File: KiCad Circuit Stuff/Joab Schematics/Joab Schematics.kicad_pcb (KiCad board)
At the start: 2 copper layers, 56 parts, among them J1 Conn_02x16_Odd_Even, J2 Conn_01x02, Q1 S8550, Q2 MMBT3904, U1 MT3608, U2 AMS1117-3.3, U3 TP4056, U4 INA219AIDCNR, U6 TS5A3159DCKR, U7 TPS5430DDAR

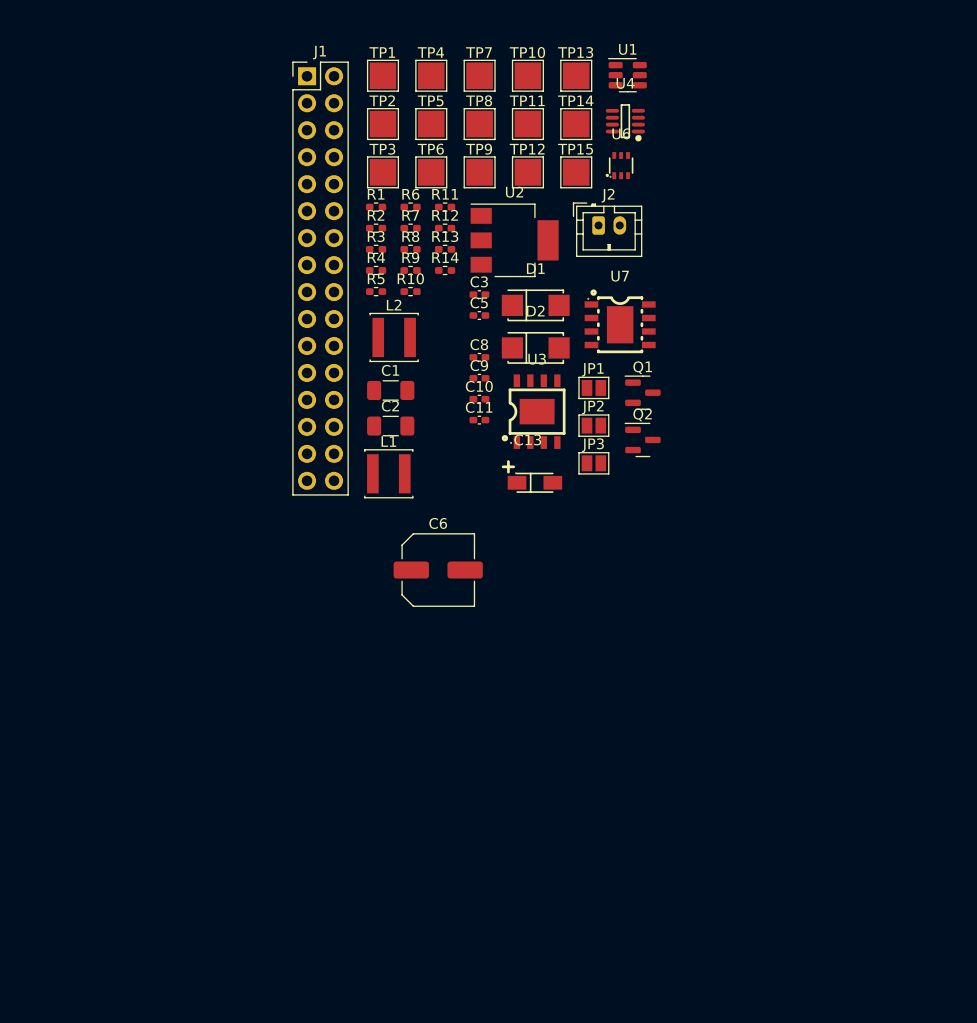
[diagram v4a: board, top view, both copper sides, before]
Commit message: Chose all passive components, added test points to all
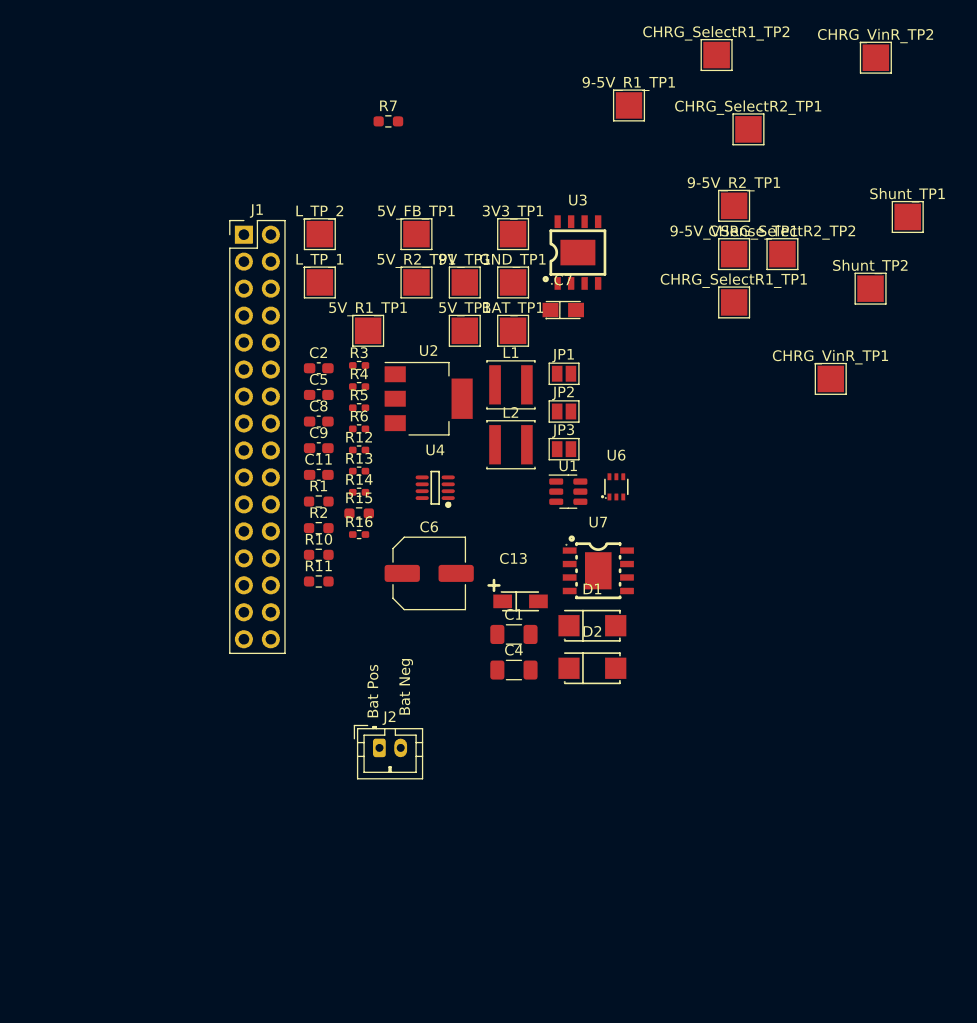
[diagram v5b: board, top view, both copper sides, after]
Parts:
- removed C10, C3: 10u, Capacitor_SMD:C_0402_1005Metric_Pad0.74x0.62mm_HandSolder
- removed Q1: S8550, Package_TO_SOT_SMD:SOT-23
- removed Q2: MMBT3904, Package_TO_SOT_SMD:SOT-23
- removed R8: 2k, Resistor_SMD:R_0402_1005Metric_Pad0.72x0.64mm_HandSolder
- removed R9: 1000k, Resistor_SMD:R_0402_1005Metric_Pad0.72x0.64mm_HandSolder
- removed TP1: L TP 2, TestPoint:TestPoint_Pad_2.5x2.5mm
- removed TP10, TP3, TP4, TP5, TP6, TP7, TP8, TP9: TestPoint, TestPoint:TestPoint_Pad_2.5x2.5mm
- removed TP11: 9V TP, TestPoint:TestPoint_Pad_2.5x2.5mm
- removed TP12: 5V TP, TestPoint:TestPoint_Pad_2.5x2.5mm
- removed TP13: 3V3 TP, TestPoint:TestPoint_Pad_2.5x2.5mm
- removed TP14: GND TP, TestPoint:TestPoint_Pad_2.5x2.5mm
- removed TP15: BAT TP, TestPoint:TestPoint_Pad_2.5x2.5mm
- removed TP2: L TP 1, TestPoint:TestPoint_Pad_2.5x2.5mm
- added 3V3_TP1: 3V3 TP, TestPoint:TestPoint_Pad_2.5x2.5mm, F.Cu at (174.6, 75.4)
- added 5V_FB_TP1: 5V FB TP, TestPoint:TestPoint_Pad_2.5x2.5mm, F.Cu at (165.5, 75.4)
- added 5V_R1_TP1: ~, TestPoint:TestPoint_Pad_2.5x2.5mm, F.Cu at (160.9, 84.5)
- added 5V_R2_TP1: 5V R2 TP, TestPoint:TestPoint_Pad_2.5x2.5mm, F.Cu at (165.5, 79.9)
- added 5V_TP1: 5V TP, TestPoint:TestPoint_Pad_2.5x2.5mm, F.Cu at (170.0, 84.5)
- added 9-5V_R1_TP1: 9-5V R1 TP, TestPoint:TestPoint_Pad_2.5x2.5mm, F.Cu at (185.5, 63.2)
- added 9-5V_R2_TP1: 9-5V R2 TP, TestPoint:TestPoint_Pad_2.5x2.5mm, F.Cu at (195.4, 72.7)
- added 9-5V_VSense_TP1: 9-5V VSense TP, TestPoint:TestPoint_Pad_2.5x2.5mm, F.Cu at (195.4, 77.2)
- added 9V_TP1: 9V TP, TestPoint:TestPoint_Pad_2.5x2.5mm, F.Cu at (170.0, 79.9)
- added BAT_TP1: BAT TP, TestPoint:TestPoint_Pad_2.5x2.5mm, F.Cu at (174.6, 84.5)
- added C4: 22u, Capacitor_SMD:C_1206_3216Metric_Pad1.33x1.80mm_HandSolder, F.Cu at (174.7, 116.4)
- added C7: CA45-A-10V-22UF-K, JLCPCB:CASE-A_3216, F.Cu at (179.3, 82.5)
- added CHRG_SelectR1_TP1: TestPoint, TestPoint:TestPoint_Pad_2.5x2.5mm, F.Cu at (195.4, 81.8)
- added CHRG_SelectR1_TP2: TestPoint, TestPoint:TestPoint_Pad_2.5x2.5mm, F.Cu at (193.8, 58.5)
- added CHRG_SelectR2_TP1: TestPoint, TestPoint:TestPoint_Pad_2.5x2.5mm, F.Cu at (196.8, 65.5)
- added CHRG_SelectR2_TP2: TestPoint, TestPoint:TestPoint_Pad_2.5x2.5mm, F.Cu at (199.9, 77.2)
- added CHRG_VinR_TP1: TestPoint, TestPoint:TestPoint_Pad_2.5x2.5mm, F.Cu at (204.5, 89.0)
- added CHRG_VinR_TP2: TestPoint, TestPoint:TestPoint_Pad_2.5x2.5mm, F.Cu at (208.8, 58.8)
- added GND_TP1: GND TP, TestPoint:TestPoint_Pad_2.5x2.5mm, F.Cu at (174.6, 79.9)
- added L_TP_1: ~, TestPoint:TestPoint_Pad_2.5x2.5mm, F.Cu at (156.4, 79.9)
- added L_TP_2: ~, TestPoint:TestPoint_Pad_2.5x2.5mm, F.Cu at (156.4, 75.4)
- added R15: 2.2R, Resistor_SMD:R_0603_1608Metric_Pad0.98x0.95mm_HandSolder, F.Cu at (160.1, 101.7)
- added R16: 2.2k, Resistor_SMD:R_0402_1005Metric_Pad0.72x0.64mm_HandSolder, F.Cu at (160.1, 103.7)
- added Shunt_TP1: TestPoint, TestPoint:TestPoint_Pad_2.5x2.5mm, F.Cu at (211.8, 73.8)
- added Shunt_TP2: TestPoint, TestPoint:TestPoint_Pad_2.5x2.5mm, F.Cu at (208.2, 80.5)
- C11: value 0.1u -> 100p; footprint Capacitor_SMD:C_0402_1005Metric_Pad0.74x0.62mm_HandSolder -> Capacitor_SMD:C_0603_1608Metric_Pad1.08x0.95mm_HandSolder
- C2: value 22u -> 10u; footprint Capacitor_SMD:C_1206_3216Metric_Pad1.33x1.80mm_HandSolder -> Capacitor_SMD:C_0603_1608Metric_Pad1.08x0.95mm_HandSolder
- C5: value 0.01u -> 10p; footprint Capacitor_SMD:C_0402_1005Metric_Pad0.74x0.62mm_HandSolder -> Capacitor_SMD:C_0603_1608Metric_Pad1.08x0.95mm_HandSolder
- C8, C9: footprint Capacitor_SMD:C_0402_1005Metric_Pad0.74x0.62mm_HandSolder -> Capacitor_SMD:C_0603_1608Metric_Pad1.08x0.95mm_HandSolder
- R1: value 680k -> 220k; footprint Resistor_SMD:R_0402_1005Metric_Pad0.72x0.64mm_HandSolder -> Resistor_SMD:R_0603_1608Metric_Pad0.98x0.95mm_HandSolder
- R10, R11: footprint Resistor_SMD:R_0402_1005Metric_Pad0.72x0.64mm_HandSolder -> Resistor_SMD:R_0603_1608Metric_Pad0.98x0.95mm_HandSolder
- R12: value 0.1R -> 100m
- R14: value 5.5k -> 3.3k
- R2: value 56k -> 22k; footprint Resistor_SMD:R_0402_1005Metric_Pad0.72x0.64mm_HandSolder -> Resistor_SMD:R_0603_1608Metric_Pad0.98x0.95mm_HandSolder
- R3: value 100k -> 33k
- R4: value 3.3k -> 2.2k
- R6: value 180k -> 1k
- R7: value 5.5k -> 4.7R; footprint Resistor_SMD:R_0402_1005Metric_Pad0.72x0.64mm_HandSolder -> Resistor_SMD:R_0603_1608Metric_Pad0.98x0.95mm_HandSolder
- moved J2 53.4 mm to (162.0, 123.8)
- moved U1 39.6 mm to (179.8, 99.6)
- moved U4 38.9 mm to (167.2, 99.2)
- moved R11 37.2 mm to (156.3, 108.1)
- moved D1 30.6 mm to (182.1, 112.2)
- moved D2 30.6 mm to (182.1, 116.2)
- moved U6 30.3 mm to (184.3, 99.2)
- moved R2 28.8 mm to (156.3, 103.1)
- moved R1 28.2 mm to (156.3, 100.5)
- moved R10 26.3 mm to (156.3, 105.6)
- moved C1 25.7 mm to (174.7, 113.1)
- moved U7 23.3 mm to (182.6, 107.1)
- moved R12 22.4 mm to (160.1, 95.7)
- moved R13 22.4 mm to (160.1, 97.7)
- moved R14 22.4 mm to (160.1, 99.7)
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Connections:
- C2 pad 1: /Battery_Out -> GND
- C2 pad 2: GND -> /Battery_Out_Before_Switch
- C9 pad 1: GND -> Net-(C9-Pad1)
- J1 pad 14: /Battery -> /Battery_In
- JP2 pad 2: /Battery_Out -> /Battery_Out_Before_Switch
- L1 pad 1: /Battery_Out -> /Battery_Out_After_Switch
- R10 pad 1: /Battery_Out -> /Battery_Out_Before_Switch
- R12 pad 1: /Battery_Out -> /Battery_Out_Before_Switch
- R14 pad 2: GND -> Net-(R14-Pad2)
- R4 pad 2: GND -> Net-(R4-Pad2)
- R6 pad 1: Net-(U7-VSENSE) -> GND
- R6 pad 2: GND -> Net-(R4-Pad2)
- R7 pad 1: Net-(Q1-E) -> Net-(C9-Pad1)
- U1 pad 4: /Battery_Out -> /Battery_Out_After_Switch
- U1 pad 5: /Battery_Out -> /Battery_Out_After_Switch
- U3 pad 5: /Battery_Out -> /Battery_Out_Before_Switch
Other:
- board text added: "Bat Neg"
- board text added: "Bat Pos"
